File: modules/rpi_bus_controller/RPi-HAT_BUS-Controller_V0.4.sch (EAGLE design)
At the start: 69 parts, among them IC1 MC34063AD, IC2 ADUM1201ARZ, IC3 P89LPC922FDH,512FDH, IC4 24LC-I/OT, IC5 LPC1115, Q1 ASF1, T1 BC856, T2 BCP52, T3 BC847

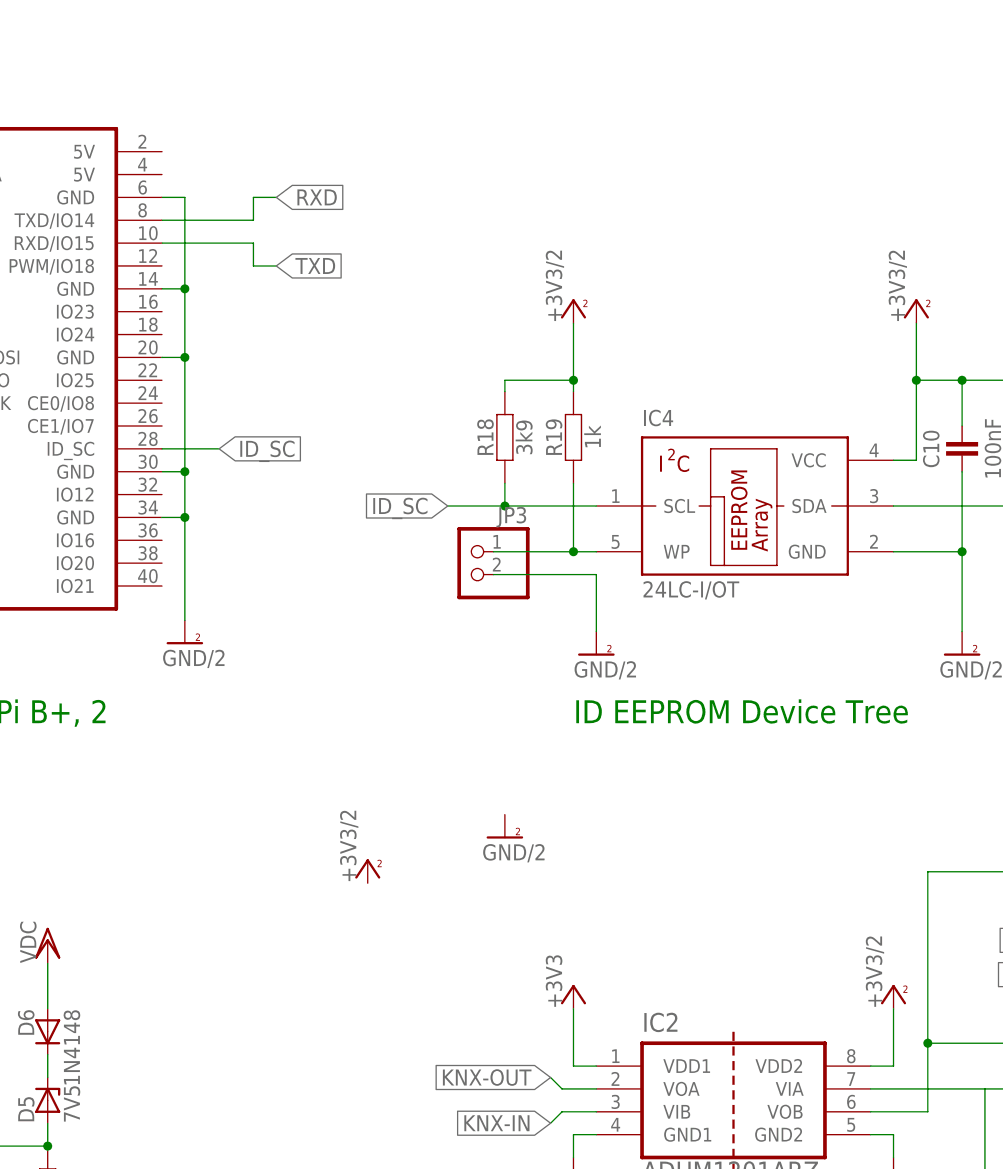
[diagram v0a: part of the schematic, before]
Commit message: Add TX/RX resistors and decoupling capacitors for ADUM.
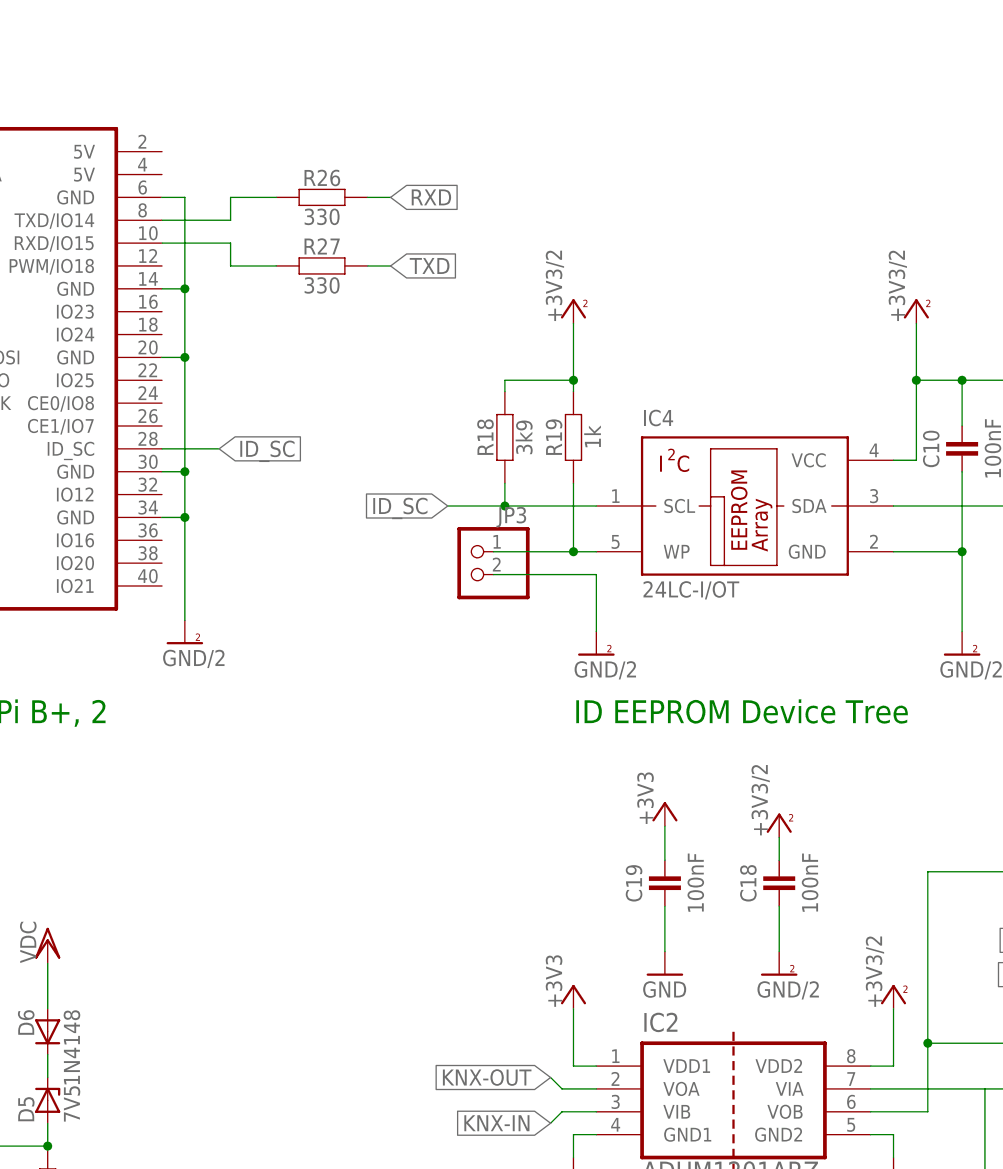
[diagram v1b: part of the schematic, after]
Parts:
- added C18, C19: 100nF, RCL_for_Selfbus-Projects:CAPACITORC1206
- added R26, R27: 330, RCL_for_Selfbus-Projects:RESISTORR1206
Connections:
- new net N$15: R26.2
- new net N$16: R27.2
- new net N$17: JP2.TXD/IO14, R26.1
- new net N$18: JP2.RXD/IO15, R27.1
- net +3V3: now also C19.2
- net +3V3/2: now also C18.2
- net GND: now also C19.1
- net GND/2: now also C18.1
- net RXD: no longer JP2.TXD/IO14
- net TXD: no longer JP2.RXD/IO15
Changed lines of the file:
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@@
 <?xml version="1.0" encoding="utf-8"?>
 <!DOCTYPE eagle SYSTEM "eagle.dtd">
-<eagle version="7.4.0">
+<eagle version="6.5.0">
 <drawing>
 <settings>
@@
 <setting verticaltext="up"/>
 </settings>
-<grid distance="0.05" unitdist="inch" unit="inch" style="lines" multiple="1" display="no" altdistance="0.01" altunitdist="inch" altunit="inch"/>
+<grid distance="0.1" unitdist="inch" unit="inch" style="lines" multiple="1" display="no" altdistance="0.01" altunitdist="inch" altunit="inch"/>
 <layers>
 <layer number="1" name="Top" color="4" fill="1" visible="no" active="no"/>
@@
 <part name="R25" library="RCL_for_Selfbus-Projects" deviceset="RESISTOR" device="R1206" value="1k"/>
 <part name="GNDI6" library="Supply_for_Selfbus-Projects" deviceset="GND/2" device=""/>
+<part name="C18" library="RCL_for_Selfbus-Projects" deviceset="CAPACITOR" device="C1206" value="100nF"/>
+<part name="GND6" library="Supply_for_Selfbus-Projects" deviceset="GND" device=""/>
+<part name="C19" library="RCL_for_Selfbus-Projects" deviceset="CAPACITOR" device="C1206" value="100nF"/>
+<part name="+3V4" library="Supply_for_Selfbus-Projects" deviceset="+3V3" device=""/>
+<part name="R26" library="RCL_for_Selfbus-Projects" deviceset="RESISTOR" device="R1206" value="330"/>
+<part name="R27" library="RCL_for_Selfbus-Projects" deviceset="RESISTOR" device="R1206" value="330"/>
 </parts>
 <sheets>
@@
 <instance part="C10" gate="G$1" x="254" y="119.38" rot="R90"/>
 <instance part="JP3" gate="G$1" x="199.39" y="105.41" rot="MR0"/>
-<instance part="P+11" gate="1" x="187.96" y="71.12"/>
-<instance part="GNDI10" gate="G$1" x="203.2" y="76.2"/>
+<instance part="P+11" gate="1" x="233.68" y="76.2"/>
+<instance part="GNDI10" gate="G$1" x="233.68" y="60.96"/>
 <instance part="P+12" gate="1" x="246.38" y="57.15"/>
 <instance part="P+13" gate="1" x="331.47" y="68.58"/>
@@
 <instance part="R25" gate="G$1" x="312.42" y="29.21" rot="R90"/>
 <instance part="GNDI6" gate="G$1" x="312.42" y="17.78"/>
+<instance part="C18" gate="G$1" x="233.68" y="71.12" rot="R90"/>
+<instance part="GND6" gate="1" x="220.98" y="60.96"/>
+<instance part="C19" gate="G$1" x="220.98" y="71.12" rot="R90"/>
+<instance part="+3V4" gate="G$1" x="220.98" y="77.47"/>
+<instance part="R26" gate="G$1" x="182.88" y="147.32"/>
+<instance part="R27" gate="G$1" x="182.88" y="139.7"/>
 </instances>
 <busses>
@@
 <wire x1="210.82" y1="50.8" x2="210.82" y2="57.15" width="0.1524" layer="91"/>
 </segment>
+<segment>
+<pinref part="C19" gate="G$1" pin="2"/>
+<wire x1="220.98" y1="73.66" x2="220.98" y2="77.47" width="0.1524" layer="91"/>
+<pinref part="+3V4" gate="G$1" pin="+3V3"/>
+</segment>
 </net>
 <net name="SDA" class="0">
@@
 <wire x1="266.7" y1="63.5" x2="265.43" y2="64.77" width="0.1524" layer="91"/>
 <label x="265.43" y="64.77" size="1.778" layer="95" rot="R180" xref="yes"/>
-<label x="177.8" y="139.7" size="1.778" layer="95" xref="yes"/>
+<label x="190.5" y="139.7" size="1.778" layer="95" xref="yes"/>
 </segment>
 <segment>
@@
 <pinref part="R23" gate="G$1" pin="2"/>
 </segment>
-<segment>
-<pinref part="JP2" gate="G$1" pin="RXD/IO15"/>
-<wire x1="165.1" y1="142.24" x2="175.26" y2="142.24" width="0.1524" layer="91"/>
-<wire x1="175.26" y1="142.24" x2="175.26" y2="139.7" width="0.1524" layer="91"/>
-<wire x1="175.26" y1="139.7" x2="177.8" y2="139.7" width="0.1524" layer="91"/>
-</segment>
 </net>
 <net name="RXD" class="0">
@@
 <wire x1="267.97" y1="60.96" x2="265.43" y2="60.96" width="0.1524" layer="91"/>
 <label x="265.43" y="60.96" size="1.778" layer="95" rot="R180" xref="yes"/>
-<label x="177.8" y="147.32" size="1.778" layer="95" xref="yes"/>
+<label x="190.5" y="147.32" size="1.778" layer="95" xref="yes"/>
 </segment>
 <segment>
@@
 <pinref part="IC5" gate="G$1" pin="PIO3_1/DSR/CT16B0_MAT1/RXD"/>
 <wire x1="533.4" y1="86.36" x2="525.78" y2="86.36" width="0.1524" layer="91"/>
-</segment>
-<segment>
-<pinref part="JP2" gate="G$1" pin="TXD/IO14"/>
-<wire x1="165.1" y1="144.78" x2="175.26" y2="144.78" width="0.1524" layer="91"/>
-<wire x1="175.26" y1="144.78" x2="175.26" y2="147.32" width="0.1524" layer="91"/>
-<wire x1="175.26" y1="147.32" x2="177.8" y2="147.32" width="0.1524" layer="91"/>
 </segment>
 </net>
@@
 <wire x1="210.82" y1="43.18" x2="210.82" y2="40.64" width="0.1524" layer="91"/>
 </segment>
+<segment>
+<pinref part="GND6" gate="1" pin="GND"/>
+<pinref part="C19" gate="G$1" pin="1"/>
+<wire x1="220.98" y1="63.5" x2="220.98" y2="68.58" width="0.1524" layer="91"/>
+</segment>
 </net>
 <net name="+3V3/2" class="0">
@@
 <junction x="528.32" y="68.58"/>
 <pinref part="P+7" gate="1" pin="+3V3/2"/>
+</segment>
+<segment>
+<pinref part="C18" gate="G$1" pin="2"/>
+<pinref part="P+11" gate="1" pin="+3V3/2"/>
+<wire x1="233.68" y1="73.66" x2="233.68" y2="76.2" width="0.1524" layer="91"/>
 </segment>
 </net>
@@
 <wire x1="312.42" y1="20.32" x2="312.42" y2="24.13" width="0.1524" layer="91"/>
 </segment>
+<segment>
+<pinref part="GNDI10" gate="G$1" pin="GND/2"/>
+<pinref part="C18" gate="G$1" pin="1"/>
+<wire x1="233.68" y1="63.5" x2="233.68" y2="68.58" width="0.1524" layer="91"/>
+</segment>
 </net>
 <net name="EIB_IN" class="0">
@@
 </segment>
 </net>
+<net name="N$15" class="0">
+<segment>
+<pinref part="R26" gate="G$1" pin="2"/>
+<wire x1="187.96" y1="147.32" x2="190.5" y2="147.32" width="0.1524" layer="91"/>
+</segment>
+</net>
+<net name="N$16" class="0">
+<segment>
+<pinref part="R27" gate="G$1" pin="2"/>
+<wire x1="187.96" y1="139.7" x2="190.5" y2="139.7" width="0.1524" layer="91"/>
+</segment>
+</net>
+<net name="N$17" class="0">
+<segment>
+<pinref part="JP2" gate="G$1" pin="TXD/IO14"/>
+<wire x1="165.1" y1="144.78" x2="172.72" y2="144.78" width="0.1524" layer="91"/>
+<wire x1="172.72" y1="144.78" x2="172.72" y2="147.32" width="0.1524" layer="91"/>
+<pinref part="R26" gate="G$1" pin="1"/>
+<wire x1="172.72" y1="147.32" x2="177.8" y2="147.32" width="0.1524" layer="91"/>
+</segment>
+</net>
+<net name="N$18" class="0">
+<segment>
+<pinref part="JP2" gate="G$1" pin="RXD/IO15"/>
+<wire x1="165.1" y1="142.24" x2="172.72" y2="142.24" width="0.1524" layer="91"/>
+<wire x1="172.72" y1="142.24" x2="172.72" y2="139.7" width="0.1524" layer="91"/>
+<pinref part="R27" gate="G$1" pin="1"/>
+<wire x1="172.72" y1="139.7" x2="177.8" y2="139.7" width="0.1524" layer="91"/>
+</segment>
+</net>
